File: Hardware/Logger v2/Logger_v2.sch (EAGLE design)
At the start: 87 parts, among them IC1 24AA256SN, J6 5.5x2.1mm Barrel, Q5 4.3A/20V/54mΩ, Q6 4.3A/20V/54mΩ, Q7 4.3A/20V/54mΩ, Q8 220mA/50V/3.5Ω, Q9 220mA/50V/3.5Ω, U1 ATSAMD21G-A, U3 915MHz, U4 SX1509

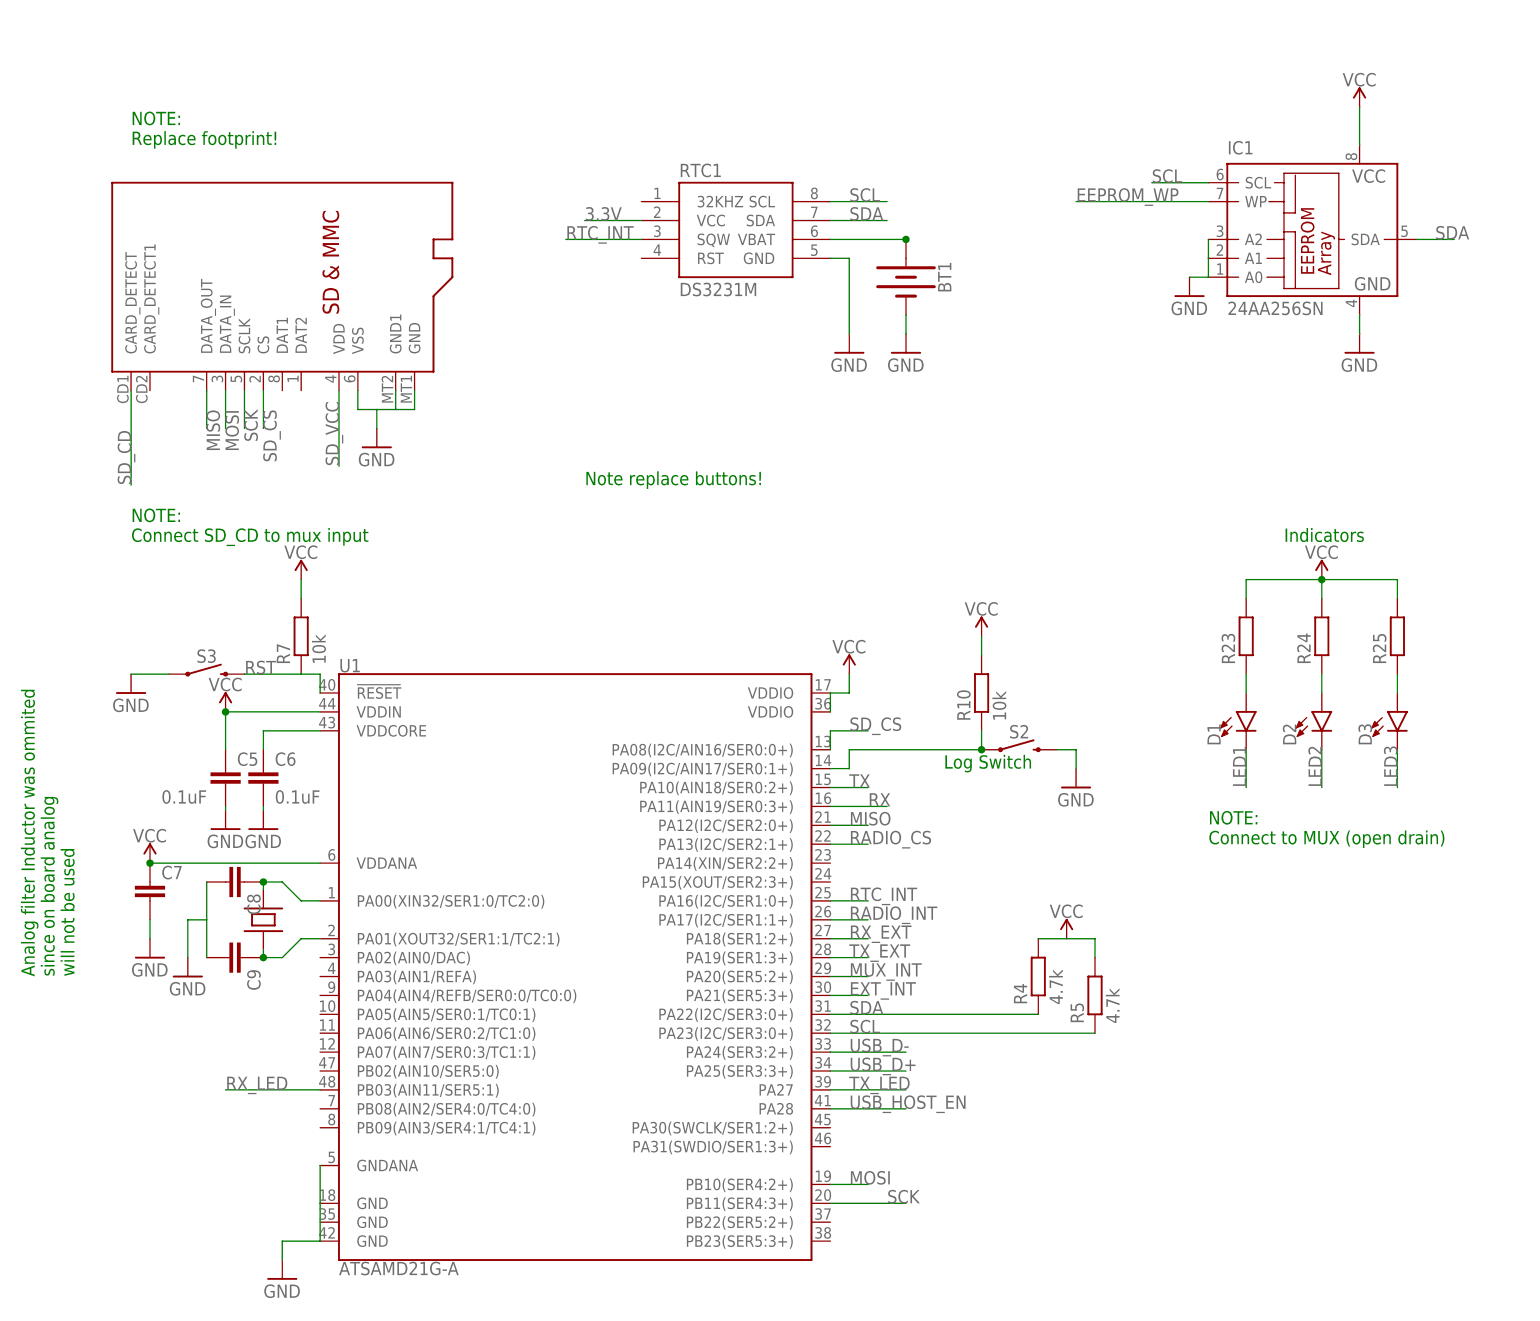
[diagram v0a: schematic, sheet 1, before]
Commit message: PCB Major Issues Fixed
All major issues on the PCB are fixed and only remaining problems are with solder mask spacing. Ready for final functional check
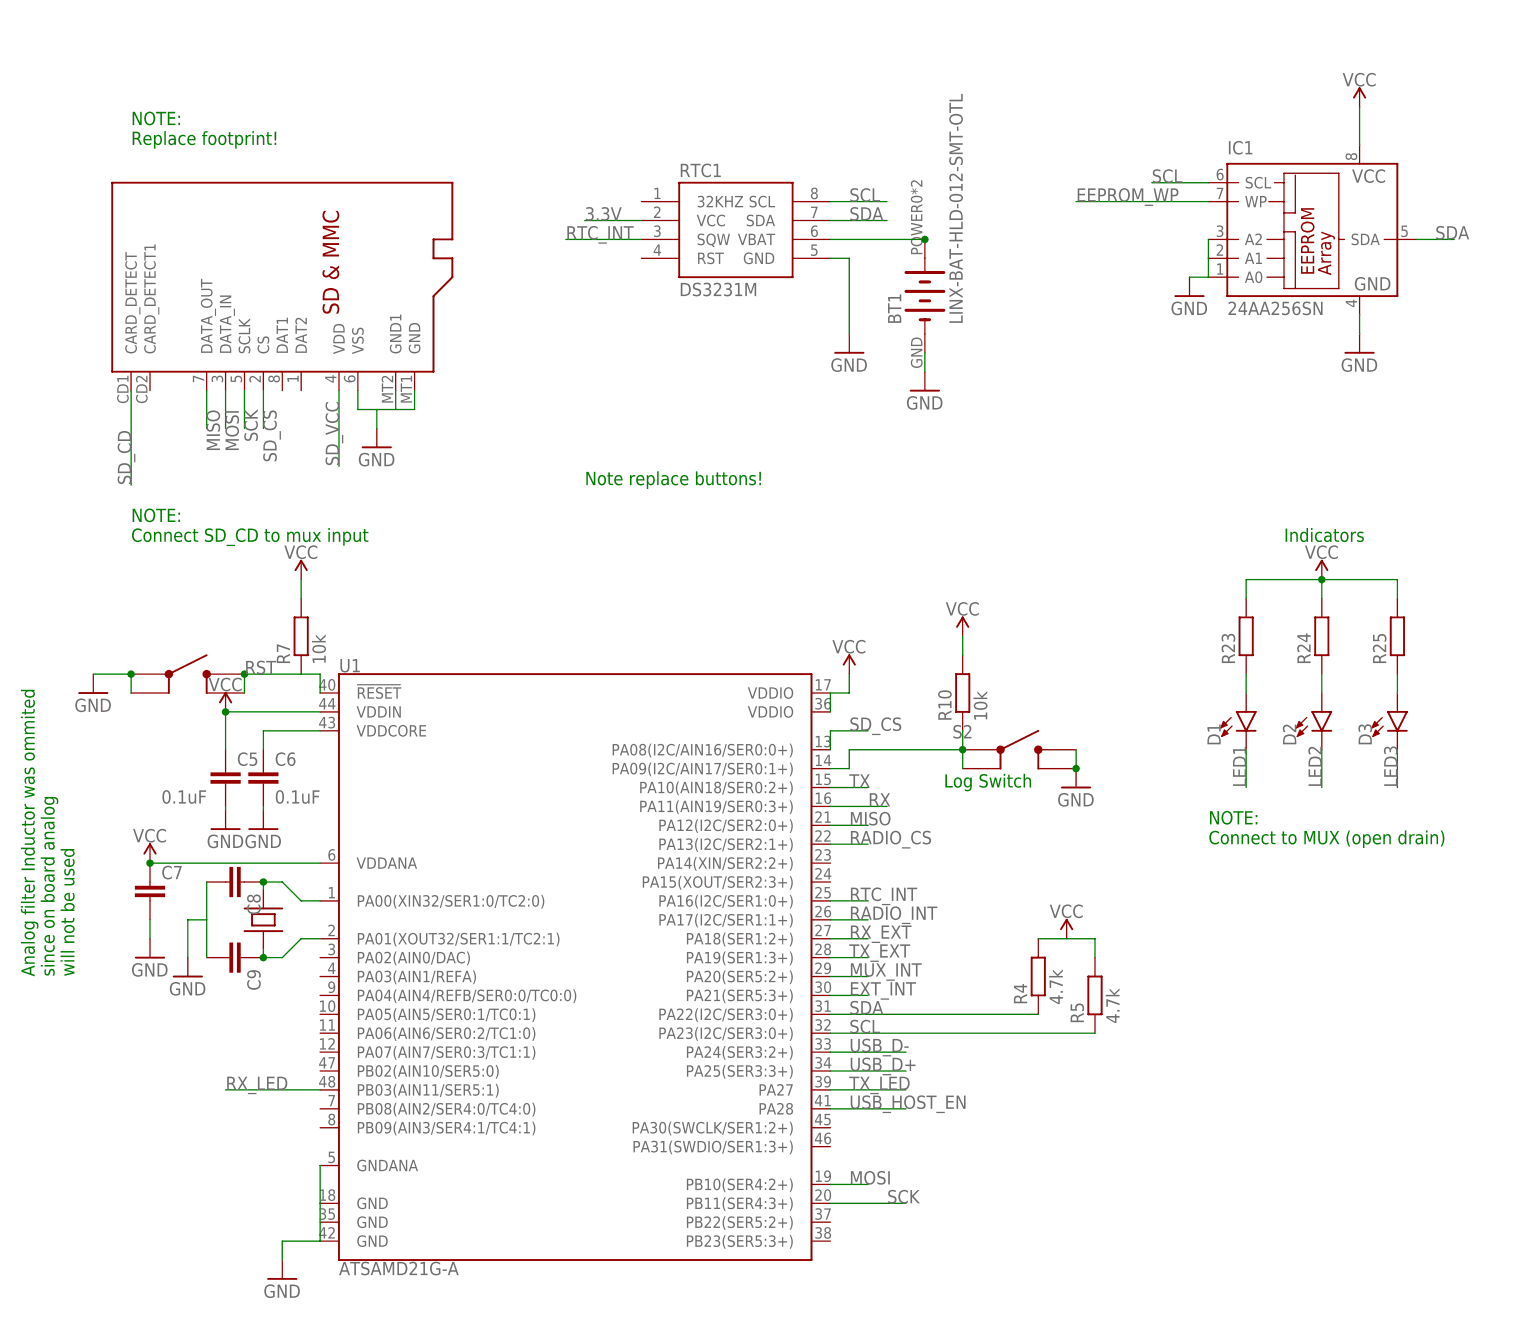
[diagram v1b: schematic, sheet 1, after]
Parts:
- removed S3: MOMENTARY-SWITCH-SPST-SMD-5.2MM, SparkFun-Switches:MOMENTARY-SWITCH-SPST-SMD-5.2MM
- added U$1: SKRPABE010, Custom:SKRPABE010
- BT1: value (none) -> LINX-BAT-HLD-012-SMT-OTL; device SparkFun-Batteries:BATTERY-12MM_SMD -> awickert:LINX-BAT-HLD-012-SMT-OTL
- S2: value MOMENTARY-SWITCH-SPST-SMD-5.2MM -> SKRPABE010; device SparkFun-Switches:MOMENTARY-SWITCH-SPST-SMD-5.2MM -> Custom:SKRPABE010
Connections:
- net GND: now also S2.3, S2.4, U$1.1, U$1.2; no longer S2.2, S3.1
- net N$5: now also S2.2
- net RST: now also U$1.3, U$1.4; no longer S3.2
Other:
- moved on the sheet: R10
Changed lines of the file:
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@@
 <part name="Q7" library="SparkFun-DiscreteSemi" deviceset="MOSFET_PCH" device="-IRLML2244" value="4.3A/20V/54mΩ"/>
 <part name="R22" library="rcl" deviceset="R-EU_" device="R0603" value="10k"/>
-<part name="BT1" library="SparkFun-Batteries" deviceset="BATTERY" device="-12MM_SMD"/>
+<part name="BT1" library="awickert" deviceset="LINX-BAT-HLD-012-SMT-OTL" device=""/>
 <part name="GND24" library="supply1" deviceset="GND" device=""/>
 <part name="GND25" library="supply1" deviceset="GND" device=""/>
@@
 <part name="J5" library="SparkFun-Connectors" deviceset="CONN_10" device=""/>
 <part name="J6" library="SparkFun-Connectors" deviceset="POWER_JACK" device="SMD" value="5.5x2.1mm Barrel"/>
-<part name="S2" library="SparkFun-Switches" deviceset="MOMENTARY-SWITCH-SPST" device="-SMD-5.2MM"/>
-<part name="S3" library="SparkFun-Switches" deviceset="MOMENTARY-SWITCH-SPST" device="-SMD-5.2MM"/>
+<part name="S2" library="Custom" deviceset="SKRPABE010" device=""/>
 <part name="J7" library="SparkFun-Connectors" deviceset="CONN_06" device="SMD-STRAIGHT-FEMALE"/>
 <part name="J11" library="SparkFun-Connectors" deviceset="CONN_06" device="SMD-STRAIGHT-FEMALE"/>
@@
 <part name="R13" library="rcl" deviceset="R-EU_" device="R0603"/>
 <part name="R14" library="rcl" deviceset="R-EU_" device="R0603"/>
+<part name="U$1" library="Custom" deviceset="SKRPABE010" device=""/>
 </parts>
 <sheets>
@@
 <text x="22.86" y="218.44" size="1.778" layer="91">NOTE:
 Replace footprint!</text>
-<text x="132.08" y="134.62" size="1.778" layer="91">Log Switch</text>
+<text x="132.08" y="132.08" size="1.778" layer="91">Log Switch</text>
 <text x="15.24" y="106.68" size="1.778" layer="91" rot="R90">Analog filter Inductor was ommited
 since on board analog
@@
 <instance part="C9" gate="G$1" x="38.1" y="109.22" rot="R270"/>
 <instance part="GND14" gate="1" x="30.48" y="106.68"/>
-<instance part="GND17" gate="1" x="22.86" y="144.78"/>
+<instance part="GND17" gate="1" x="17.78" y="144.78"/>
 <instance part="GND18" gate="1" x="55.88" y="177.8"/>
 <instance part="GND19" gate="1" x="187.96" y="190.5"/>
 <instance part="GND20" gate="1" x="165.1" y="198.12"/>
-<instance part="BT1" gate="G$1" x="127" y="200.66" rot="R270"/>
-<instance part="GND24" gate="1" x="127" y="190.5"/>
+<instance part="BT1" gate="G$1" x="129.54" y="198.12" rot="R90"/>
+<instance part="GND24" gate="1" x="129.54" y="185.42"/>
 <instance part="GND25" gate="1" x="119.38" y="190.5"/>
 <instance part="D1" gate="G$1" x="172.72" y="142.24"/>
@@
 <instance part="SUPPLY7" gate="G$1" x="119.38" y="147.32"/>
 <instance part="GND35" gate="1" x="149.86" y="132.08"/>
-<instance part="R10" gate="G$1" x="137.16" y="144.78" rot="R90"/>
-<instance part="SUPPLY15" gate="G$1" x="137.16" y="152.4"/>
-<instance part="S2" gate="G$1" x="142.24" y="137.16" smashed="yes">
-<attribute name="NAME" x="142.24" y="138.684" size="1.778" layer="95" font="vector" align="bottom-center"/>
+<instance part="R10" gate="G$1" x="134.62" y="144.78" rot="R90"/>
+<instance part="SUPPLY15" gate="G$1" x="134.62" y="152.4"/>
+<instance part="S2" gate="G$1" x="134.62" y="137.16" smashed="yes">
+<attribute name="NAME" x="134.62" y="138.684" size="1.778" layer="95" font="vector" align="bottom-center"/>
 </instance>
-<instance part="S3" gate="G$1" x="33.02" y="147.32" smashed="yes">
-<attribute name="NAME" x="33.02" y="148.844" size="1.778" layer="95" font="vector" align="bottom-center"/>
-</instance>
+<instance part="U$1" gate="G$1" x="22.86" y="147.32"/>
 </instances>
 <busses>
@@
 <pinref part="R10" gate="G$1" pin="2"/>
 <pinref part="SUPPLY15" gate="G$1" pin="VCC"/>
-<wire x1="137.16" y1="152.4" x2="137.16" y2="149.86" width="0.1524" layer="91"/>
+<wire x1="134.62" y1="152.4" x2="134.62" y2="149.86" width="0.1524" layer="91"/>
 </segment>
 </net>
@@
 <segment>
 <pinref part="GND17" gate="1" pin="GND"/>
-<wire x1="27.94" y1="147.32" x2="22.86" y2="147.32" width="0.1524" layer="91"/>
-<pinref part="S3" gate="G$1" pin="1"/>
+<pinref part="U$1" gate="G$1" pin="1"/>
+<junction x="22.86" y="147.32"/>
+<wire x1="22.86" y1="147.32" x2="17.78" y2="147.32" width="0.1524" layer="91"/>
+<pinref part="U$1" gate="G$1" pin="2"/>
+<wire x1="22.86" y1="144.78" x2="22.86" y2="147.32" width="0.1524" layer="91"/>
 </segment>
 <segment>
@@
 <pinref part="GND24" gate="1" pin="GND"/>
 <pinref part="BT1" gate="G$1" pin="-"/>
-<wire x1="127" y1="193.04" x2="127" y2="195.58" width="0.1524" layer="91"/>
+<wire x1="129.54" y1="187.96" x2="129.54" y2="190.5" width="0.1524" layer="91"/>
 </segment>
 <segment>
@@
 </segment>
 <segment>
-<wire x1="147.32" y1="137.16" x2="149.86" y2="137.16" width="0.1524" layer="91"/>
 <pinref part="GND35" gate="1" pin="GND"/>
+<pinref part="S2" gate="G$1" pin="4"/>
+<junction x="149.86" y="134.62"/>
+<pinref part="S2" gate="G$1" pin="3"/>
 <wire x1="149.86" y1="137.16" x2="149.86" y2="134.62" width="0.1524" layer="91"/>
-<pinref part="S2" gate="G$1" pin="2"/>
 </segment>
 </net>
@@
 <wire x1="38.1" y1="147.32" x2="45.72" y2="147.32" width="0.1524" layer="91"/>
 <label x="38.1" y="147.32" size="1.778" layer="95"/>
-<pinref part="S3" gate="G$1" pin="2"/>
+<pinref part="U$1" gate="G$1" pin="3"/>
+<pinref part="U$1" gate="G$1" pin="4"/>
+<wire x1="38.1" y1="144.78" x2="38.1" y2="147.32" width="0.1524" layer="91"/>
+<junction x="38.1" y="147.32"/>
 </segment>
 </net>
@@
 <wire x1="116.84" y1="134.62" x2="119.38" y2="134.62" width="0.1524" layer="91"/>
 <wire x1="119.38" y1="134.62" x2="119.38" y2="137.16" width="0.1524" layer="91"/>
-<wire x1="119.38" y1="137.16" x2="137.16" y2="137.16" width="0.1524" layer="91"/>
+<wire x1="119.38" y1="137.16" x2="134.62" y2="137.16" width="0.1524" layer="91"/>
 <pinref part="R10" gate="G$1" pin="1"/>
-<wire x1="137.16" y1="139.7" x2="137.16" y2="137.16" width="0.1524" layer="91"/>
+<wire x1="134.62" y1="139.7" x2="134.62" y2="137.16" width="0.1524" layer="91"/>
 <pinref part="S2" gate="G$1" pin="1"/>
-<junction x="137.16" y="137.16"/>
+<junction x="134.62" y="137.16"/>
+<pinref part="S2" gate="G$1" pin="2"/>
+<wire x1="134.62" y1="137.16" x2="134.62" y2="134.62" width="0.1524" layer="91"/>
 </segment>
 </net>
@@
 <segment>
 <pinref part="RTC1" gate="G$1" pin="VBAT"/>
-<wire x1="116.84" y1="205.74" x2="127" y2="205.74" width="0.1524" layer="91"/>
+<wire x1="116.84" y1="205.74" x2="129.54" y2="205.74" width="0.1524" layer="91"/>
 <pinref part="BT1" gate="G$1" pin="+"/>
-<junction x="127" y="205.74"/>
-</segment>
-</net>
+<junction x="129.54" y="205.74"/>
+</segment>
+</net>

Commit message: Final PCB Logger Design
The final design iteration for the logger PCB
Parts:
- C18: value (none) -> .1uF
- C7: value (none) -> 1uF
- C8, C9: value (none) -> 12nF
- R13, R14, R16, R17: value (none) -> FB
- R23, R24, R25: value (none) -> 330
- R44, R45, R46, R47: value (none) -> 10k
- U3: device SparkFun-RF:RFM69CW-915MHZ -> SparkFun-RF:RFM69HCW-915
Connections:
- removed net EEPROM_WP: IC1.WP
- net GND: now also IC1.WP, U1.GND@35
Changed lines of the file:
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@@
 <part name="R7" library="rcl" deviceset="R-EU_" device="R0603" value="10k"/>
 <part name="GND11" library="supply1" deviceset="GND" device=""/>
-<part name="C7" library="rcl" deviceset="C-EU" device="C0603"/>
+<part name="C7" library="rcl" deviceset="C-EU" device="C0603" value="1uF"/>
 <part name="GND13" library="supply1" deviceset="GND" device=""/>
 <part name="U$5" library="Custom" deviceset="CM200" device=""/>
-<part name="C8" library="rcl" deviceset="C-EU" device="C0603"/>
-<part name="C9" library="rcl" deviceset="C-EU" device="C0603"/>
+<part name="C8" library="rcl" deviceset="C-EU" device="C0603" value="12nF"/>
+<part name="C9" library="rcl" deviceset="C-EU" device="C0603" value="12nF"/>
 <part name="GND14" library="supply1" deviceset="GND" device=""/>
 <part name="C10" library="rcl" deviceset="C-EU" device="C0603" value="0.1uF"/>
@@
 <part name="GND19" library="supply1" deviceset="GND" device=""/>
 <part name="GND20" library="supply1" deviceset="GND" device=""/>
-<part name="U3" library="SparkFun-RF" deviceset="RFM69" device="CW-915MHZ" value="915MHz"/>
+<part name="U3" library="SparkFun-RF" deviceset="RFM69H" device="CW-915" value="915MHz"/>
 <part name="U$6" library="Custom" deviceset="UBLOX_MAX-8" device=""/>
 <part name="X1" library="adafruit" deviceset="SMACONNECTOR" device="_EDGE"/>
-<part name="R16" library="rcl" deviceset="R-EU_" device="R0603"/>
-<part name="R17" library="rcl" deviceset="R-EU_" device="R0603"/>
+<part name="R16" library="rcl" deviceset="R-EU_" device="R0603" value="FB"/>
+<part name="R17" library="rcl" deviceset="R-EU_" device="R0603" value="FB"/>
 <part name="Q5" library="SparkFun-DiscreteSemi" deviceset="MOSFET_PCH" device="-IRLML2244" value="4.3A/20V/54mΩ"/>
 <part name="R20" library="rcl" deviceset="R-EU_" device="R0603" value="10k"/>
@@
 <part name="D2" library="SparkFun-LED" deviceset="LED" device="0603"/>
 <part name="D3" library="SparkFun-LED" deviceset="LED" device="0603"/>
-<part name="R23" library="rcl" deviceset="R-EU_" device="R0603"/>
-<part name="R24" library="rcl" deviceset="R-EU_" device="R0603"/>
-<part name="R25" library="rcl" deviceset="R-EU_" device="R0603"/>
+<part name="R23" library="rcl" deviceset="R-EU_" device="R0603" value="330"/>
+<part name="R24" library="rcl" deviceset="R-EU_" device="R0603" value="330"/>
+<part name="R25" library="rcl" deviceset="R-EU_" device="R0603" value="330"/>
 <part name="GND26" library="supply1" deviceset="GND" device=""/>
 <part name="GND27" library="supply1" deviceset="GND" device=""/>
@@
 <part name="R42" library="rcl" deviceset="R-EU_" device="R0603" value="10k"/>
 <part name="R43" library="rcl" deviceset="R-EU_" device="R0603" value="10k"/>
-<part name="R44" library="rcl" deviceset="R-EU_" device="R0603"/>
-<part name="R45" library="rcl" deviceset="R-EU_" device="R0603"/>
+<part name="R44" library="rcl" deviceset="R-EU_" device="R0603" value="10k"/>
+<part name="R45" library="rcl" deviceset="R-EU_" device="R0603" value="10k"/>
 <part name="GND21" library="supply1" deviceset="GND" device=""/>
-<part name="R46" library="rcl" deviceset="R-EU_" device="R0603"/>
-<part name="R47" library="rcl" deviceset="R-EU_" device="R0603"/>
+<part name="R46" library="rcl" deviceset="R-EU_" device="R0603" value="10k"/>
+<part name="R47" library="rcl" deviceset="R-EU_" device="R0603" value="10k"/>
 <part name="GND22" library="supply1" deviceset="GND" device=""/>
 <part name="U4" library="SparkFun-IC-Special-Function" deviceset="SX1509" device="" value="SX1509"/>
@@
 <part name="R11" library="rcl" deviceset="R-EU_" device="R0603" value="10k"/>
 <part name="R12" library="rcl" deviceset="R-EU_" device="R0603" value="10k"/>
-<part name="C18" library="rcl" deviceset="C-EU" device="C0603"/>
-<part name="R13" library="rcl" deviceset="R-EU_" device="R0603"/>
-<part name="R14" library="rcl" deviceset="R-EU_" device="R0603"/>
+<part name="C18" library="rcl" deviceset="C-EU" device="C0603" value=".1uF"/>
+<part name="R13" library="rcl" deviceset="R-EU_" device="R0603" value="FB"/>
+<part name="R14" library="rcl" deviceset="R-EU_" device="R0603" value="FB"/>
 <part name="U$1" library="Custom" deviceset="SKRPABE010" device=""/>
+<part name="GND36" library="supply1" deviceset="GND" device=""/>
 </parts>
 <sheets>
@@
 </instance>
 <instance part="U$1" gate="G$1" x="22.86" y="147.32"/>
+<instance part="GND36" gate="1" x="157.48" y="205.74"/>
 </instances>
 <busses>
@@
 <pinref part="U1" gate="G$1" pin="GND@18"/>
 <pinref part="U1" gate="G$1" pin="GND@42"/>
-<wire x1="48.26" y1="76.2" x2="48.26" y2="71.12" width="0.1524" layer="91"/>
+<wire x1="48.26" y1="76.2" x2="48.26" y2="73.66" width="0.1524" layer="91"/>
+<wire x1="48.26" y1="73.66" x2="48.26" y2="71.12" width="0.1524" layer="91"/>
 <wire x1="48.26" y1="71.12" x2="43.18" y2="71.12" width="0.1524" layer="91"/>
 <pinref part="GND11" gate="1" pin="GND"/>
@@
 <pinref part="U1" gate="G$1" pin="GNDANA"/>
 <wire x1="48.26" y1="81.28" x2="48.26" y2="76.2" width="0.1524" layer="91"/>
+<pinref part="U1" gate="G$1" pin="GND@35"/>
+<junction x="48.26" y="73.66"/>
+<junction x="48.26" y="76.2"/>
 </segment>
 <segment>
@@
 <wire x1="149.86" y1="137.16" x2="149.86" y2="134.62" width="0.1524" layer="91"/>
 </segment>
+<segment>
+<pinref part="IC1" gate="G$1" pin="WP"/>
+<wire x1="167.64" y1="210.82" x2="157.48" y2="210.82" width="0.1524" layer="91"/>
+<label x="149.86" y="210.82" size="1.778" layer="95"/>
+<pinref part="GND36" gate="1" pin="GND"/>
+<wire x1="157.48" y1="210.82" x2="149.86" y2="210.82" width="0.1524" layer="91"/>
+<wire x1="157.48" y1="208.28" x2="157.48" y2="210.82" width="0.1524" layer="91"/>
+<junction x="157.48" y="210.82"/>
+</segment>
 </net>
 <net name="RST" class="0">
@@
 <wire x1="116.84" y1="139.7" x2="121.92" y2="139.7" width="0.1524" layer="91"/>
 <label x="119.38" y="139.7" size="1.778" layer="95"/>
-</segment>
-</net>
-<net name="EEPROM_WP" class="0">
-<segment>
-<pinref part="IC1" gate="G$1" pin="WP"/>
-<wire x1="167.64" y1="210.82" x2="149.86" y2="210.82" width="0.1524" layer="91"/>
-<label x="149.86" y="210.82" size="1.778" layer="95"/>
 </segment>
 </net>
@@
 <segment>
 <pinref part="U3" gate="G$1" pin="DIO0"/>
-<wire x1="45.72" y1="43.18" x2="53.34" y2="43.18" width="0.1524" layer="91"/>
+<wire x1="45.72" y1="45.72" x2="53.34" y2="43.18" width="0.1524" layer="91"/>
 <label x="48.26" y="43.18" size="1.778" layer="95"/>
 </segment>
@@
 <segment>
 <pinref part="U3" gate="G$1" pin="3.3V"/>
-<wire x1="20.32" y1="43.18" x2="5.08" y2="43.18" width="0.1524" layer="91"/>
+<wire x1="20.32" y1="45.72" x2="5.08" y2="43.18" width="0.1524" layer="91"/>
 <label x="5.08" y="43.18" size="1.778" layer="95"/>
 </segment>
